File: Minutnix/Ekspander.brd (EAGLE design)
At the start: 215.2 x 44.1 mm, 14 parts, among them X1 FH12-12S-0.5SH, X6 JST-XH-03-PIN-LONG-PAD

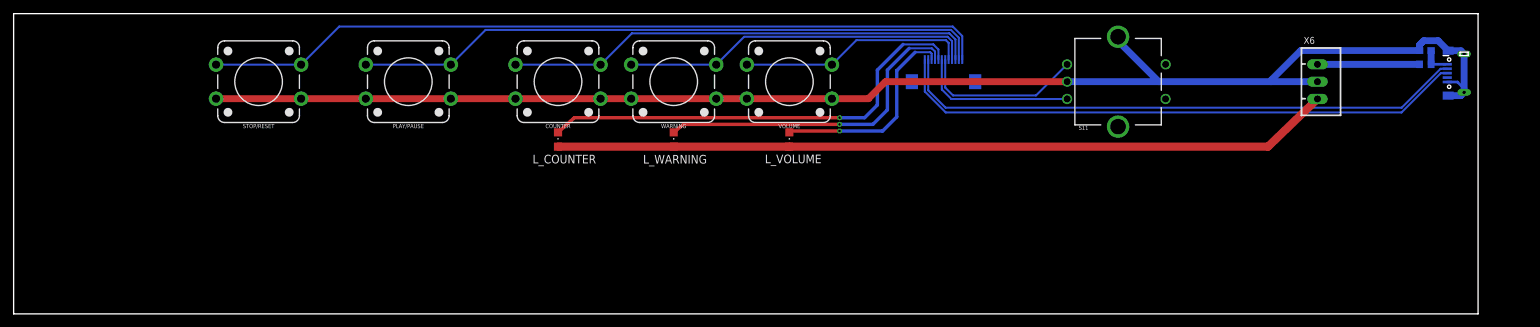
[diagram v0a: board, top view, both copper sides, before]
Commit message: libs actualisation + drc rules for expander
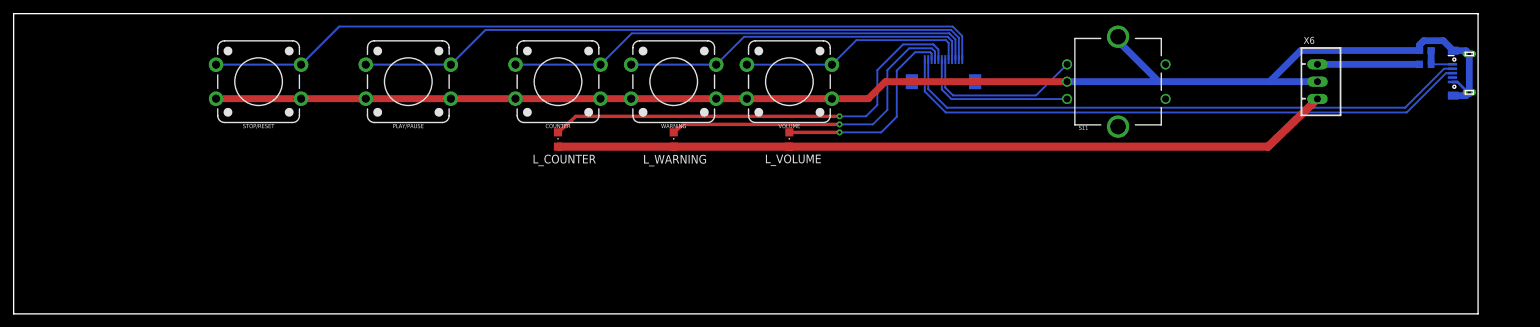
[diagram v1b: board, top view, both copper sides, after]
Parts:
- X1: value FH12-12S-0.5SH -> FH12-12S-0.5S_THINNER; device con-hirose:FH12-12S-0.5SH -> My_con-hirose:FH12-12S-0.5SH_THINER
- moved U$1 0.76 mm to (214.2, -8.75)
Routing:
- net GND: track 215.3 -> 272.6 mm
- net VCC: track 114.4 -> 131.4 mm
- net N$9: track 85.1 -> 85.9 mm
- net N$7: track 84.2 -> 84.9 mm
- net N$14: track 4.44 -> 4.96 mm

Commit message: Probably final routing of Expander board
DRC 8mils clean
libs actualisation
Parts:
- PLAY/PAUSE: device SparkFun-Switches:TACTILE_SWITCH_PTH_12MM -> MySparkFun-Switches:TACTILE_SWITCH_PTH_12MM
- moved S11 24.7 mm to (187.0, -10.0)
- moved X6 21.6 mm to (170.0, -10.0), flipped to the bottom
- moved X1 18.1 mm to (154.8, -11.2)
- moved STOP/RESET 15.0 mm to (21.0, -10.0)
- moved PLAY/PAUSE 10.0 mm to (48.0, -10.0)
- moved COUNTER 5.00 mm to (75.0, -10.0)
- moved L_COUNTER 5.00 mm to (75.0, -18.5)
- moved L_WARNING 2.00 mm to (95.0, -18.5)
- moved WARNING 2.00 mm to (95.0, -10.0)
- moved L_VOLUME 1.00 mm to (115.0, -18.5)
- moved VOLUME 1.00 mm to (115.0, -10.0)
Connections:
- net +5V: now also S11.SW-
- net GND: now also COUNTER.4, PLAY/PAUSE.4, S11.P$3, S11.P$4, S11.SW+, STOP/RESET.4, VOLUME.4, WARNING.4
- net N$2: now also STOP/RESET.2
- net N$3: now also PLAY/PAUSE.2
- net N$4: now also COUNTER.2
- net N$5: now also WARNING.2
- net N$6: now also VOLUME.2
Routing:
- net N$2: track 116.0 -> 150.7 mm
- net VCC: track 131.4 -> 97.9 mm
- net N$3: track 92.9 -> 122.1 mm
- net GND: track 272.6 -> 248.1 mm
- net +5V: track 15.0 -> 38.8 mm
- net N$4: track 69.9 -> 93.6 mm
- net N$10: track 66.0 -> 86.4 mm
- net N$7: track 84.9 -> 64.5 mm
- net N$5: track 51.8 -> 72.0 mm
- net N$9: track 85.9 -> 65.7 mm
- net N$6: track 33.8 -> 50.5 mm
- net N$11: track 48.2 -> 64.9 mm
- net N$12: track 30.7 -> 43.6 mm
- net N$8: track 23.4 -> 28.0 mm
- net N$1: track 24.4 -> 26.4 mm
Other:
- board size 215.2 x 44.1 mm -> 215.2 x 22 mm

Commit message: Drc corrections
Expander board finished:

DRC 10mils chcecked except gaps between close pads in connector and usb
in connector and usb drc 8mils passed
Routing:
- net N$8: track 28.0 -> 29.2 mm
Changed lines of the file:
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@@
 <param name="mtCopper" value="0.035mm 0.035mm 0.035mm 0.035mm 0.035mm 0.035mm 0.035mm 0.035mm 0.035mm 0.035mm 0.035mm 0.035mm 0.035mm 0.035mm 0.035mm 0.035mm"/>
 <param name="mtIsolate" value="1.5mm 0.15mm 0.2mm 0.15mm 0.2mm 0.15mm 0.2mm 0.15mm 0.2mm 0.15mm 0.2mm 0.15mm 0.2mm 0.15mm 0.2mm"/>
-<param name="mdWireWire" value="8mil"/>
-<param name="mdWirePad" value="8mil"/>
-<param name="mdWireVia" value="8mil"/>
-<param name="mdPadPad" value="8mil"/>
-<param name="mdPadVia" value="8mil"/>
-<param name="mdViaVia" value="8mil"/>
-<param name="mdSmdPad" value="8mil"/>
-<param name="mdSmdVia" value="8mil"/>
-<param name="mdSmdSmd" value="8mil"/>
+<param name="mdWireWire" value="10mil"/>
+<param name="mdWirePad" value="10mil"/>
+<param name="mdWireVia" value="10mil"/>
+<param name="mdPadPad" value="10mil"/>
+<param name="mdPadVia" value="10mil"/>
+<param name="mdViaVia" value="10mil"/>
+<param name="mdSmdPad" value="10mil"/>
+<param name="mdSmdVia" value="10mil"/>
+<param name="mdSmdSmd" value="10mil"/>
 <param name="mdViaViaSameLayer" value="6mil"/>
 <param name="mnLayersViaInSmd" value="2"/>
@@
 <contactref element="X1" pad="7"/>
 <contactref element="S11" pad="B"/>
-<wire x1="179.507" y1="-12.54" x2="178.217" y2="-11.25" width="0.3048" layer="16"/>
-<wire x1="178.217" y1="-11.25" x2="162.25" y2="-11.25" width="0.3048" layer="16"/>
-<wire x1="162.25" y1="-11.25" x2="160.75" y2="-9.75" width="0.3048" layer="16"/>
-<wire x1="160.75" y1="-9.75" x2="158.39710625" y2="-9.75" width="0.3048" layer="16"/>
-<wire x1="158.14710625" y1="-10" x2="155" y2="-10" width="0.3048" layer="16"/>
-<wire x1="158.39710625" y1="-9.75" x2="158.14710625" y2="-10" width="0.3048" layer="16"/>
+<wire x1="158" y1="-13" x2="166.047" y2="-13" width="0.3048" layer="16"/>
 <wire x1="154.5" y1="-8" x2="154.5" y2="-9.5" width="0.29" layer="16"/>
-<wire x1="154.5" y1="-9.5" x2="155" y2="-10" width="0.3048" layer="16"/>
+<wire x1="154.5" y1="-9.5" x2="158" y2="-13" width="0.3048" layer="16"/>
+<wire x1="166.047" y1="-13" x2="167.797" y2="-11.25" width="0.3048" layer="16"/>
+<wire x1="178.217" y1="-11.25" x2="179.507" y2="-12.54" width="0.3048" layer="16"/>
+<wire x1="167.797" y1="-11.25" x2="178.217" y2="-11.25" width="0.3048" layer="16"/>
 </signal>
 <signal name="N$11">

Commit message: lib update + board ongoing
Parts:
- moved U$1 7.12 mm to (221.3, -9.75)
- moved L1 7.01 mm to (214.4, -8.53)
- moved C4 7.01 mm to (214.4, -6.50)
- moved X1 0.30 mm to (154.6, -11.0)
- moved WARNING 0.27 mm to (94.9, -9.75)
- moved X6 0.26 mm to (170.1, -9.75)
- moved STOP/RESET 0.26 mm to (20.9, -9.75)
- moved S11 0.25 mm to (186.9, -9.75)
- moved PLAY/PAUSE 0.25 mm to (48.0, -9.75)
- moved COUNTER 0.25 mm to (75.0, -9.75)
- moved VOLUME 0.25 mm to (115.0, -9.75)
- moved L_WARNING 0.24 mm to (94.9, -18.3)
- moved L_COUNTER 0.21 mm to (75.0, -18.3)
- moved L_VOLUME 0.21 mm to (115.0, -18.3)
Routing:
- net GND: track 248.1 -> 256.1 mm
- net +5V: track 38.8 -> 46.2 mm
- net N$7: track 64.5 -> 71.2 mm
- net N$9: track 65.7 -> 72.3 mm
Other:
- board size 215.2 x 22 mm -> 222.3 x 21.9 mm

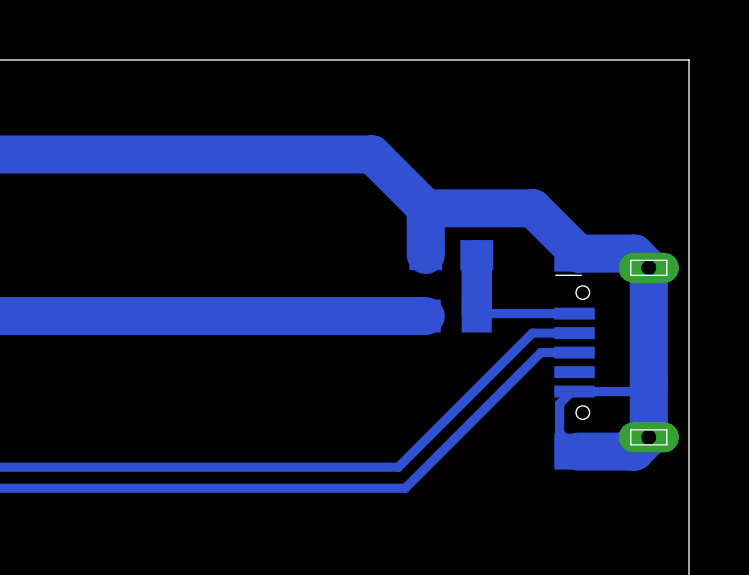
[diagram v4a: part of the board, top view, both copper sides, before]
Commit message: Final packages
+most paths wider (24 mils)
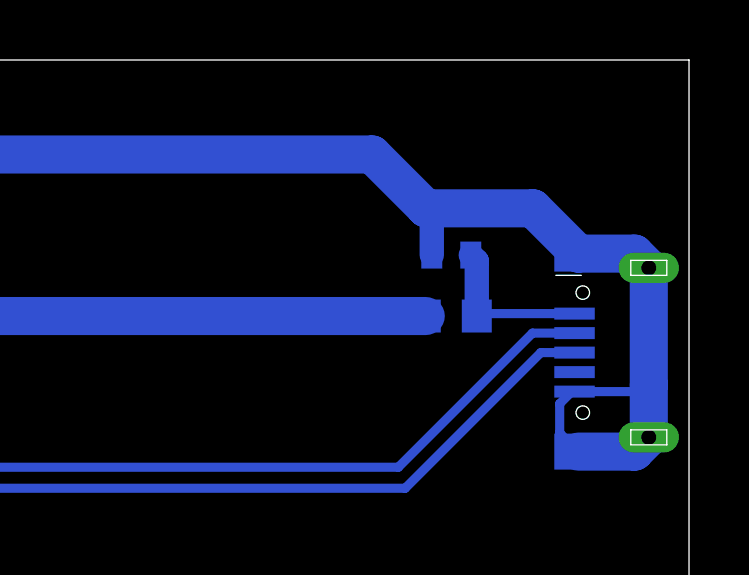
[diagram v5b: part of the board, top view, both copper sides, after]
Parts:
- C4: device rcl:C0603 -> rcl:C0402
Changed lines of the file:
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@@
 </autorouter>
 <elements>
-<element name="C4" library="rcl" library_urn="urn:adsk.eagle:library:334" package="C0603" package3d_urn="urn:adsk.eagle:package:23616/2" value="10n'" x="214.376" y="-6.5024" smashed="yes" rot="MR0">
+<element name="C4" library="rcl" library_urn="urn:adsk.eagle:library:334" package="C0402" package3d_urn="urn:adsk.eagle:package:23626/2" value="10n'" x="214.376" y="-6.5024" smashed="yes" rot="MR0">
 <attribute name="NAME" x="212.261" y="-6.9174" size="1.27" layer="26" rot="MR0"/>
 <attribute name="SPICEPREFIX" value="C" x="197.866" y="-78.8924" size="1.778" layer="28" rot="MR0" display="off"/>
@@
 <wire x1="160.25" y1="-15.75" x2="166.2464" y2="-9.7536" width="1.27" layer="1"/>
 <wire x1="166.2464" y1="-9.7536" x2="170.0784" y2="-9.7536" width="1.27" layer="1"/>
-<wire x1="213.526" y1="-6.5024" x2="213.526" y2="-4.9364" width="1.27" layer="16"/>
 <wire x1="213.526" y1="-4.9364" x2="211.7392" y2="-3.1496" width="1.27" layer="16"/>
 <wire x1="213.5338" y1="-4.9442" x2="213.526" y2="-4.9364" width="1.27" layer="16"/>
@@
 <wire x1="218.4848" y1="-11.0536" x2="220.7364" y2="-11.0536" width="0.3048" layer="16"/>
 <wire x1="220.7364" y1="-11.0536" x2="220.9598" y2="-10.8302" width="0.3048" layer="16"/>
+<wire x1="213.726" y1="-6.5024" x2="213.726" y2="-5.1364" width="0.8128" layer="16"/>
+<wire x1="213.726" y1="-5.1364" x2="213.526" y2="-4.9364" width="0.8128" layer="16"/>
 </signal>
 <signal name="N$14">
@@
 <contactref element="L1" pad="2"/>
 <contactref element="U$1" pad="1"/>
-<wire x1="215.226" y1="-6.5024" x2="215.226" y2="-8.5344" width="1.016" layer="16"/>
 <wire x1="218.4848" y1="-8.4536" x2="215.3068" y2="-8.4536" width="0.3048" layer="16"/>
 <wire x1="215.3068" y1="-8.4536" x2="215.226" y2="-8.5344" width="0.3048" layer="16"/>
+<wire x1="215.226" y1="-8.5344" x2="215.226" y2="-6.7024" width="0.8128" layer="16"/>
+<wire x1="215.226" y1="-6.7024" x2="215.026" y2="-6.5024" width="0.8128" layer="16"/>
 </signal>
 <signal name="VCC">

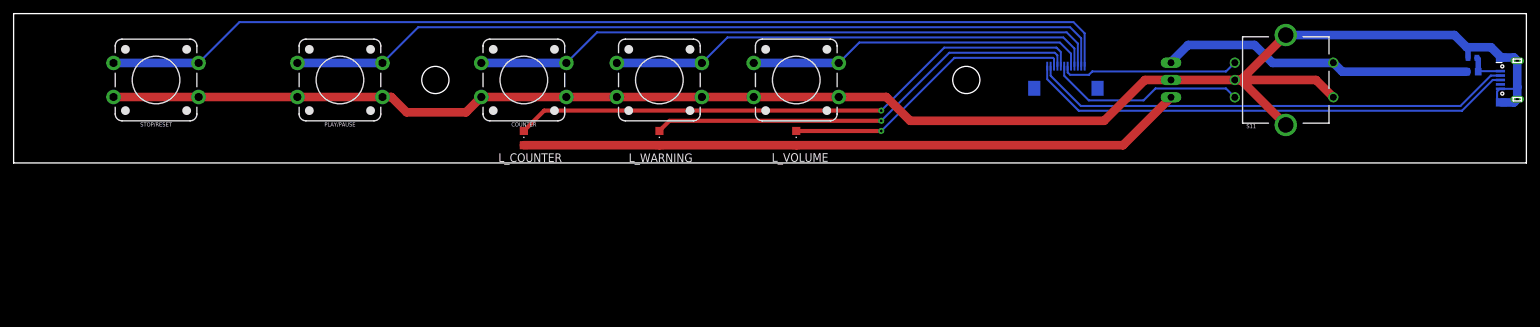
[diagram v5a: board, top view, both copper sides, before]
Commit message: rotation of tape ports
also some nets wider
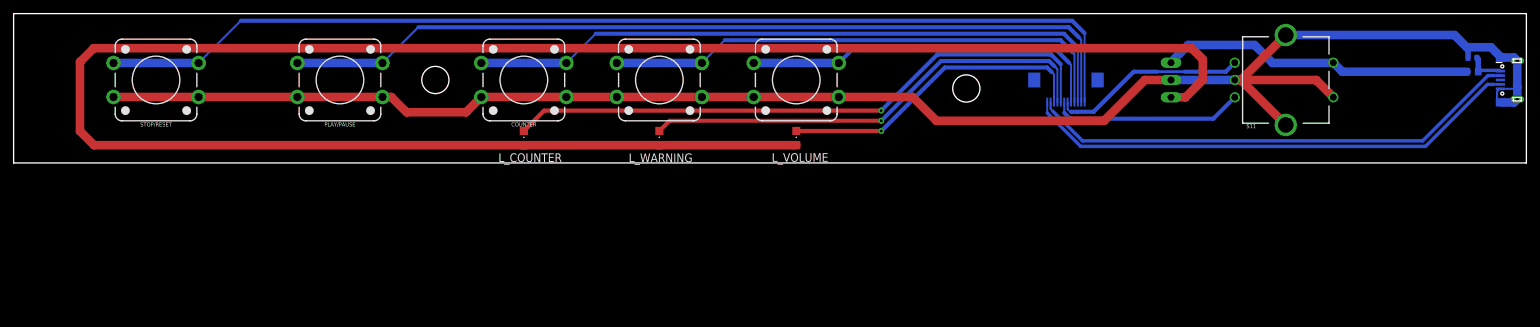
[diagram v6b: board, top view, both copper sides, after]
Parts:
- moved X1 1.22 mm to (154.6, -9.75), turned to 180 degrees
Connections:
- removed net N$8: S11.B, X1.7
- removed net N$9: U$1.3, X1.12
- new net N$17: U$1.4, X1.1
- new net N$18: U$1.2, X1.2
- net N$1: now also X1.7; no longer X1.6
- net N$10: now also X1.5; no longer X1.8
- net N$11: now also X1.4; no longer X1.9
- net N$12: now also X1.3; no longer X1.10
- net N$2: now also X1.12; no longer X1.1
- net N$3: now also X1.11; no longer X1.2
- net N$4: now also X1.10; no longer X1.3
- net N$5: now also X1.9; no longer X1.4
- net N$6: now also X1.8; no longer X1.5
- net N$7: now also S11.B, X1.6; no longer U$1.2, X1.11
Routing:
- net VCC: track 98.0 -> 291.6 mm
- net N$17: track 0.00 -> 74.0 mm
- net N$18: track 0.00 -> 73.9 mm
- net N$9: track 72.3 -> 0.00 mm
- net N$7: track 71.2 -> 28.3 mm
- net N$8: track 29.2 -> 0.00 mm
- net N$1: track 26.4 -> 32.6 mm
- net N$2: track 150.7 -> 156.2 mm
- net N$3: track 122.1 -> 127.3 mm
- net N$4: track 93.5 -> 98.3 mm
- net N$5: track 72.1 -> 76.5 mm
- net N$6: track 50.4 -> 54.0 mm
- net N$10: track 86.3 -> 89.7 mm
- net N$11: track 65.0 -> 68.1 mm
- net N$12: track 43.5 -> 46.2 mm

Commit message: expander pools
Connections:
- net GND: now also X1.CASE1, X1.CASE2
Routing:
- added copper zone on layer 1, net GND
- added copper zone on layer 16, net GND
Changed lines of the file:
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@@
 <setting verticaltext="up"/>
 </settings>
-<grid distance="8" unitdist="mil" unit="mil" style="lines" multiple="1" display="yes" altdistance="5" altunitdist="mil" altunit="mil"/>
+<grid distance="0.5" unitdist="mil" unit="mil" style="lines" multiple="1" display="yes" altdistance="5" altunitdist="mil" altunit="mil"/>
 <layers>
 <layer number="1" name="Top" color="4" fill="1" visible="yes" active="yes"/>
@@
 <layer number="14" name="Route14" color="22" fill="1" visible="no" active="no"/>
 <layer number="15" name="Route15" color="23" fill="1" visible="no" active="no"/>
-<layer number="16" name="Bottom" color="1" fill="1" visible="yes" active="yes"/>
+<layer number="16" name="Bottom" color="1" fill="1" visible="no" active="yes"/>
 <layer number="17" name="Pads" color="2" fill="1" visible="yes" active="yes"/>
 <layer number="18" name="Vias" color="2" fill="1" visible="yes" active="yes"/>
@@
 <wire x1="213.726" y1="-5.1364" x2="213.526" y2="-4.9364" width="0.8128" layer="16"/>
 <wire x1="170.0784" y1="-9.7536" x2="179.451" y2="-9.7536" width="1.27" layer="16"/>
+<polygon width="0.0254" layer="16" thermals="no">
+<vertex x="0.6096" y="-0.6096"/>
+<vertex x="221.6912" y="-0.6096"/>
+<vertex x="221.6912" y="-21.336"/>
+<vertex x="0.6096" y="-21.336"/>
+</polygon>
+<polygon width="0.1524" layer="16" pour="cutout">
+<vertex x="32.7152" y="-1.2192"/>
+<vertex x="32.7152" y="-0.4064"/>
+<vertex x="32.9184" y="-0.4064"/>
+<vertex x="33.1216" y="-0.4064"/>
+<vertex x="33.1216" y="-1.2192"/>
+</polygon>
+<polygon width="0.1524" layer="16" pour="cutout">
+<vertex x="58.7248" y="-1.4224"/>
+<vertex x="58.7248" y="-2.2352"/>
+<vertex x="59.3344" y="-2.2352"/>
+<vertex x="59.3344" y="-2.032"/>
+<vertex x="59.3344" y="-1.4224"/>
+</polygon>
+<polygon width="0.1524" layer="16" pour="cutout">
+<vertex x="84.9376" y="-2.4384"/>
+<vertex x="84.9376" y="-3.048"/>
+<vertex x="85.1408" y="-3.048"/>
+<vertex x="85.1408" y="-2.4384"/>
+</polygon>
+<polygon width="0.1524" layer="16" pour="cutout">
+<vertex x="103.8352" y="-3.4544"/>
+<vertex x="103.8352" y="-4.064"/>
+<vertex x="104.0384" y="-4.064"/>
+<vertex x="104.0384" y="-3.4544"/>
+</polygon>
+<polygon width="0.1524" layer="16" pour="cutout">
+<vertex x="122.936" y="-4.8768"/>
+<vertex x="122.936" y="-4.2672"/>
+<vertex x="123.1392" y="-4.2672"/>
+<vertex x="123.1392" y="-4.8768"/>
+</polygon>
+<polygon width="0.1524" layer="16" pour="cutout">
+<vertex x="128.2192" y="-13.4112"/>
+<vertex x="126.7968" y="-13.4112"/>
+<vertex x="126.7968" y="-17.8816"/>
+<vertex x="128.2192" y="-17.8816"/>
+</polygon>
+<contactref element="X1" pad="CASE2"/>
+<contactref element="X1" pad="CASE1"/>
+<polygon width="0.0254" layer="16" pour="cutout">
+<vertex x="168.3131" y="-7.1247"/>
+<vertex x="168.3131" y="-7.9883"/>
+<vertex x="168.1988" y="-7.9883"/>
+<vertex x="168.1988" y="-8.1407"/>
+<vertex x="171.7802" y="-8.1407"/>
+<vertex x="171.8437" y="-8.1407"/>
+<vertex x="171.8437" y="-7.0231"/>
+</polygon>
+<polygon width="0.0254" layer="16" pour="cutout">
+<vertex x="213.6267" y="-7.6581"/>
+<vertex x="215.7476" y="-7.6581"/>
+<vertex x="215.7476" y="-9.4107"/>
+<vertex x="213.7029" y="-9.4107"/>
+<vertex x="213.7029" y="-7.747"/>
+<vertex x="213.6267" y="-7.747"/>
+</polygon>
+<polygon width="0.0254" layer="16" pour="cutout">
+<vertex x="219.2274" y="-7.9502"/>
+<vertex x="219.4052" y="-8.128"/>
+<vertex x="219.4052" y="-10.7061"/>
+<vertex x="219.2655" y="-10.8458"/>
+<vertex x="219.2528" y="-10.8458"/>
+<vertex x="219.2528" y="-8.1153"/>
+<vertex x="219.1766" y="-8.0391"/>
+<vertex x="219.1766" y="-8.001"/>
+</polygon>
+<polygon width="0.0254" layer="16" pour="cutout">
+<vertex x="171.8437" y="-7.0231"/>
+<vertex x="171.8437" y="-6.6167"/>
+<vertex x="171.8183" y="-6.5913"/>
+<vertex x="171.6659" y="-6.7437"/>
+<vertex x="171.6659" y="-6.8072"/>
+<vertex x="171.6659" y="-6.858"/>
+<vertex x="171.8437" y="-7.0358"/>
+</polygon>
+<polygon width="0.0254" layer="1" isolate="0.4064" thermals="no">
+<vertex x="221.6912" y="-0.6096"/>
+<vertex x="0.6096" y="-0.6096"/>
+<vertex x="0.6096" y="-21.336"/>
+<vertex x="221.6912" y="-21.336"/>
+</polygon>
+<polygon width="0.0254" layer="1" pour="cutout" thermals="no">
+<vertex x="168.1607" y="-7.0104"/>
+<vertex x="168.1607" y="-6.0198"/>
+<vertex x="169.545" y="-6.0198"/>
+<vertex x="171.9961" y="-6.0198"/>
+<vertex x="171.9961" y="-6.9977"/>
+<vertex x="168.1607" y="-6.9977"/>
+</polygon>
+<polygon width="0.0254" layer="1" pour="cutout" thermals="no">
+<vertex x="116.0653" y="-17.8816"/>
+<vertex x="116.0653" y="-20.0787"/>
+<vertex x="115.7732" y="-20.3708"/>
+<vertex x="115.2271" y="-20.3708"/>
+<vertex x="115.2017" y="-20.3454"/>
+<vertex x="76.0349" y="-20.3454"/>
+<vertex x="74.041" y="-18.3515"/>
+<vertex x="73.9902" y="-18.3007"/>
+<vertex x="73.9902" y="-17.9705"/>
+<vertex x="78.1431" y="-13.8176"/>
+<vertex x="79.121" y="-13.8176"/>
+<vertex x="112.0013" y="-13.8176"/>
+</polygon>
 </signal>
 <signal name="N$14">

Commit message: Logos incorpoarted
+gerbers generated
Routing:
- net N$1: track 32.6 -> 28.8 mm
- net N$18: track 73.9 -> 73.0 mm
